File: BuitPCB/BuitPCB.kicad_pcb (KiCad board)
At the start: 2 copper layers, 100 x 100 mm, 7 parts, among them J1 USB_A, J2 RJ45_Abracon_ARJP11A-MASA-B-A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, U1 Teensy4.1

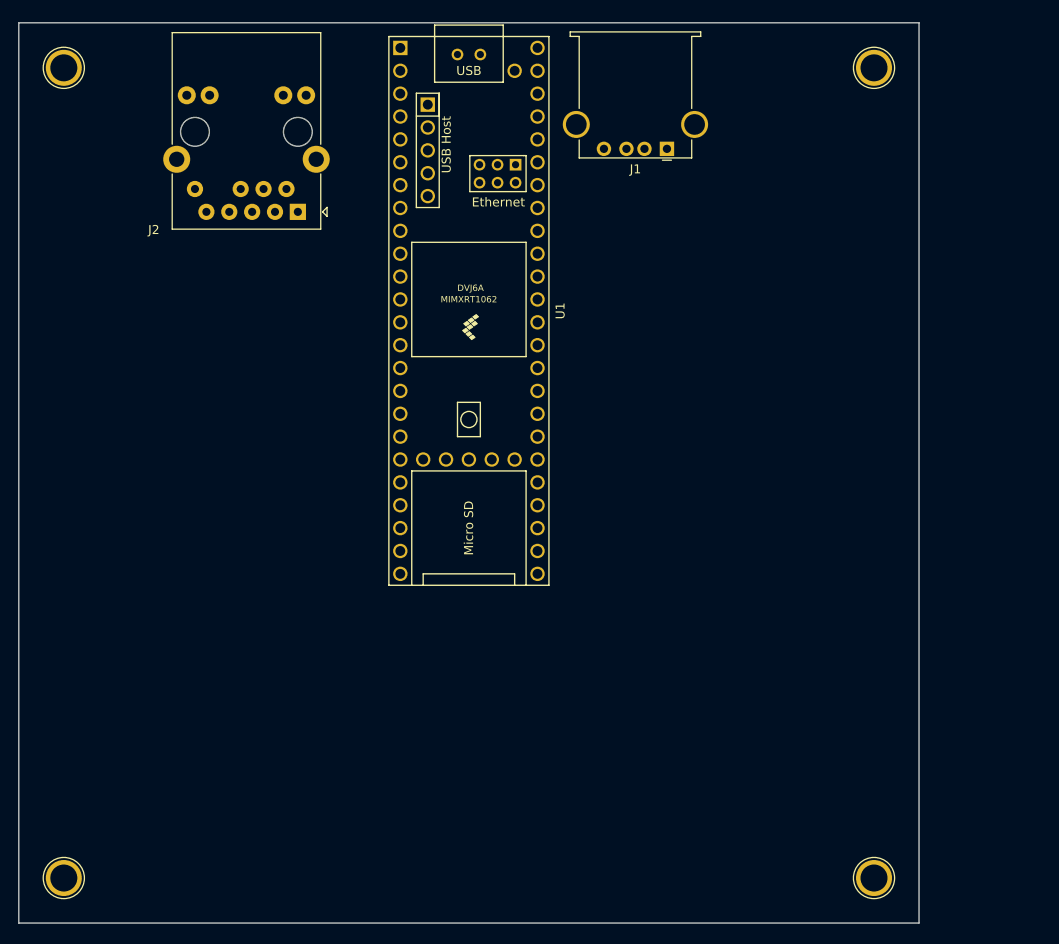
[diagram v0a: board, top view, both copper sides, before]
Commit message: Added sheets and connectors
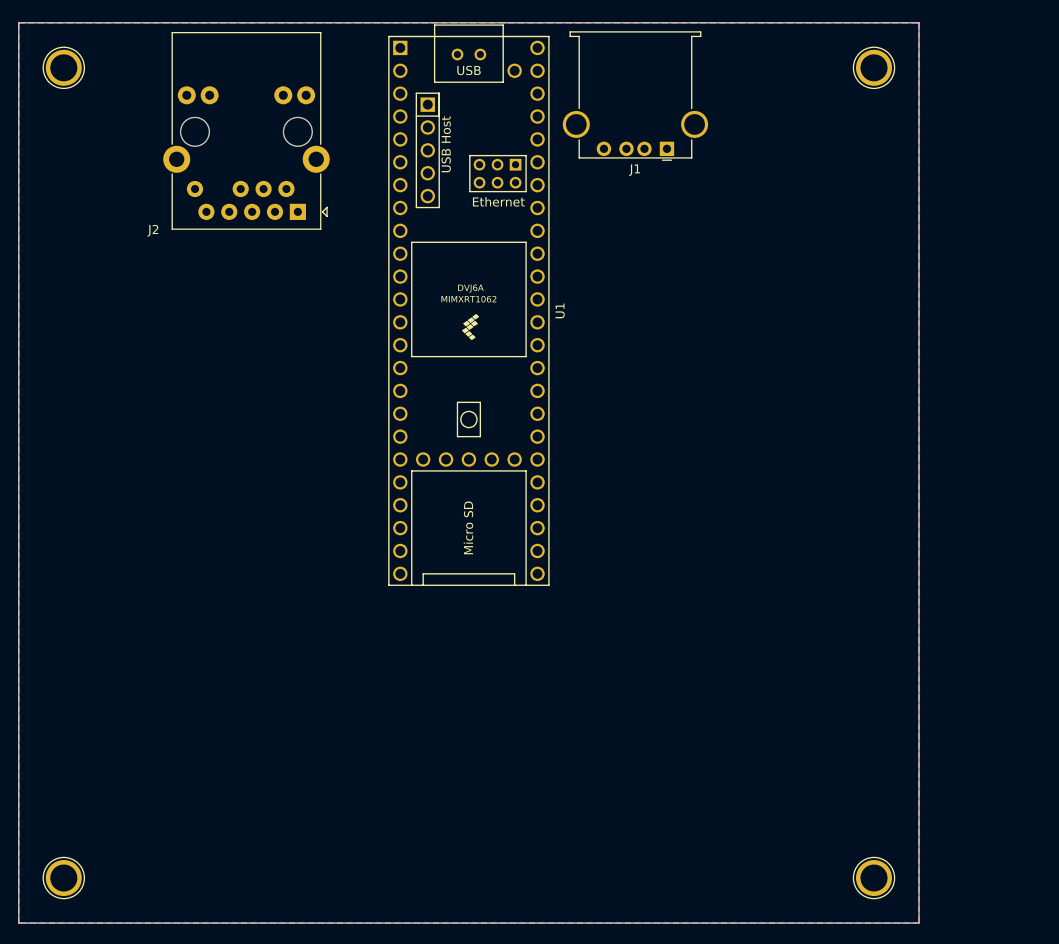
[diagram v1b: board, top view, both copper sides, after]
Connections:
- J1 pad 4: Net-(J1-Pad4) -> GND
- U1 pad 1: Net-(U1-Pad1) -> GND
- U1 pad 34: Net-(U1-Pad34) -> GND
- U1 pad 47: Net-(U1-Pad47) -> GND
- U1 pad 52: Net-(U1-Pad52) -> GND
- U1 pad 58: Net-(U1-Pad58) -> GND
- U1 pad 59: Net-(U1-Pad59) -> GND
- U1 pad 64: Net-(U1-Pad64) -> GND
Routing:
- added copper zone on B.Cu, net GND
- added copper zone on F.Cu, net GND

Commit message: Added most of components, few pending
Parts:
- removed REF** (x4): TestPoint_Plated_Hole_D3.0mm, TestPoint:TestPoint_Plated_Hole_D3.0mm
- added C1: C, Capacitor_SMD:C_0805_2012Metric, F.Cu at (178.0, 97.0)
- added C2: 100nF, Capacitor_SMD:C_0805_2012Metric, F.Cu at (176.5, 75.0)
- added C3: 100nF, Capacitor_SMD:C_0805_2012Metric, F.Cu at (181.0, 75.0)
- added C4: 100nF, Capacitor_SMD:C_0805_2012Metric, F.Cu at (176.5, 78.1)
- added D1: CD4148W, Diode_SMD:D_0805_2012Metric, F.Cu at (177.1, 110.7)
- added J10: Conn_01x06, Connector_JST:JST_XH_B6B-XH-A_1x06_P2.50mm_Vertical, F.Cu at (134.0, 117.0)
- added J11: Conn_01x04, Connector_JST:JST_XH_B4B-XH-A_1x04_P2.50mm_Vertical, F.Cu at (156.0, 126.0)
- added J12: Conn_01x04, Connector_JST:JST_XH_B4B-XH-A_1x04_P2.50mm_Vertical, F.Cu at (198.9, 122.3)
- added J13: Conn_01x04, Connector_JST:JST_XH_B4B-XH-A_1x04_P2.50mm_Vertical, F.Cu at (193.9, 130.1)
- added J14: Conn_01x04, Connector_JST:JST_XH_B4B-XH-A_1x04_P2.50mm_Vertical, F.Cu at (156.0, 136.0)
- added J15: Conn_01x04, Connector_JST:JST_XH_B4B-XH-A_1x04_P2.50mm_Vertical, F.Cu at (175.5, 134.0)
- added J16: Conn_01x04, Connector_JST:JST_XH_B4B-XH-A_1x04_P2.50mm_Vertical, F.Cu at (176.0, 124.0)
- added J17: Conn_01x04, Connector_JST:JST_XH_B4B-XH-A_1x04_P2.50mm_Vertical, F.Cu at (193.9, 137.9)
- added J18: Conn_01x04, Connector_JST:JST_XH_B4B-XH-A_1x04_P2.50mm_Vertical, F.Cu at (188.9, 145.7)
- added J3: USB_A, Connector_USB:USB_A_Stewart_SS-52100-001_Horizontal, F.Cu at (116.0, 136.0)
- added J4: AudioJack3, MiniJackConnector:MJ4435, F.Cu at (194.0, 53.0)
- added J6: AudioJack3, MiniJackConnector:MJ4435, F.Cu at (180.0, 53.0)
- added J7: Conn_01x06, Connector_JST:JST_XH_B6B-XH-A_1x06_P2.50mm_Vertical, F.Cu at (134.0, 125.0)
- added J8: Conn_01x06, Connector_JST:JST_XH_B6B-XH-A_1x06_P2.50mm_Vertical, F.Cu at (134.0, 135.0)
- added J9: Conn_01x06, Connector_JST:JST_XH_B6B-XH-A_1x06_P2.50mm_Vertical, F.Cu at (134.0, 108.0)
- added Q1: BSS138, Package_TO_SOT_SMD:SOT-23, F.Cu at (212.1, 121.2)
- added Q2: BSS138, Package_TO_SOT_SMD:SOT-23, F.Cu at (207.1, 129.0)
- added R1: 220R, Resistor_SMD:R_0805_2012Metric, F.Cu at (177.1, 113.7)
- added R2: 47R, Resistor_SMD:R_0805_2012Metric, F.Cu at (178.0, 100.0)
- added R3: 47R, Resistor_SMD:R_0805_2012Metric, F.Cu at (182.4, 97.0)
- added R4: 470R, Resistor_SMD:R_0805_2012Metric, F.Cu at (190.7, 98.8)
- added R5: 10K, Resistor_SMD:R_0805_2012Metric, F.Cu at (202.1, 143.8)
- added R6: 10K, Resistor_SMD:R_0805_2012Metric, F.Cu at (212.1, 125.0)
- added R7: 10K, Resistor_SMD:R_0805_2012Metric, F.Cu at (211.5, 128.2)
- added R8: 10K, Resistor_SMD:R_0805_2012Metric, F.Cu at (207.1, 132.8)
- added U2: 6N138, Package_DIP:DIP-8_W8.89mm_SMDSocket_LongPads, F.Cu at (136.0, 76.0)
- added U3: AP7361C-33E, Package_TO_SOT_SMD:SOT-223-3_TabPin2, F.Cu at (141.2, 95.0)
- added U4: SGTL5000XNAA3, Package_DFN_QFN:QFN-32-1EP_5x5mm_P0.5mm_EP3.6x3.6mm, F.Cu at (185.0, 86.0)
- J1: value USB_A -> DIN-5_180degree; footprint Connector_USB:USB_A_Stewart_SS-52100-001_Horizontal -> esp32s2:DJ005
- J2: value RJ45_Abracon_ARJP11A-MASA-B-A-EMU2 -> DIN-5_180degree; footprint Connector_RJ:RJ45_Abracon_ARJP11A-MA_Horizontal -> esp32s2:DJ005
- moved J1 38.6 mm to (136.0, 50.0), turned to 0 degrees
- moved J2 29.0 mm to (111.0, 50.0), turned to 0 degrees
- moved U1 11.0 mm to (161.0, 82.0)
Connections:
- J1 pad 4: GND -> Net-(J1-Pad4)

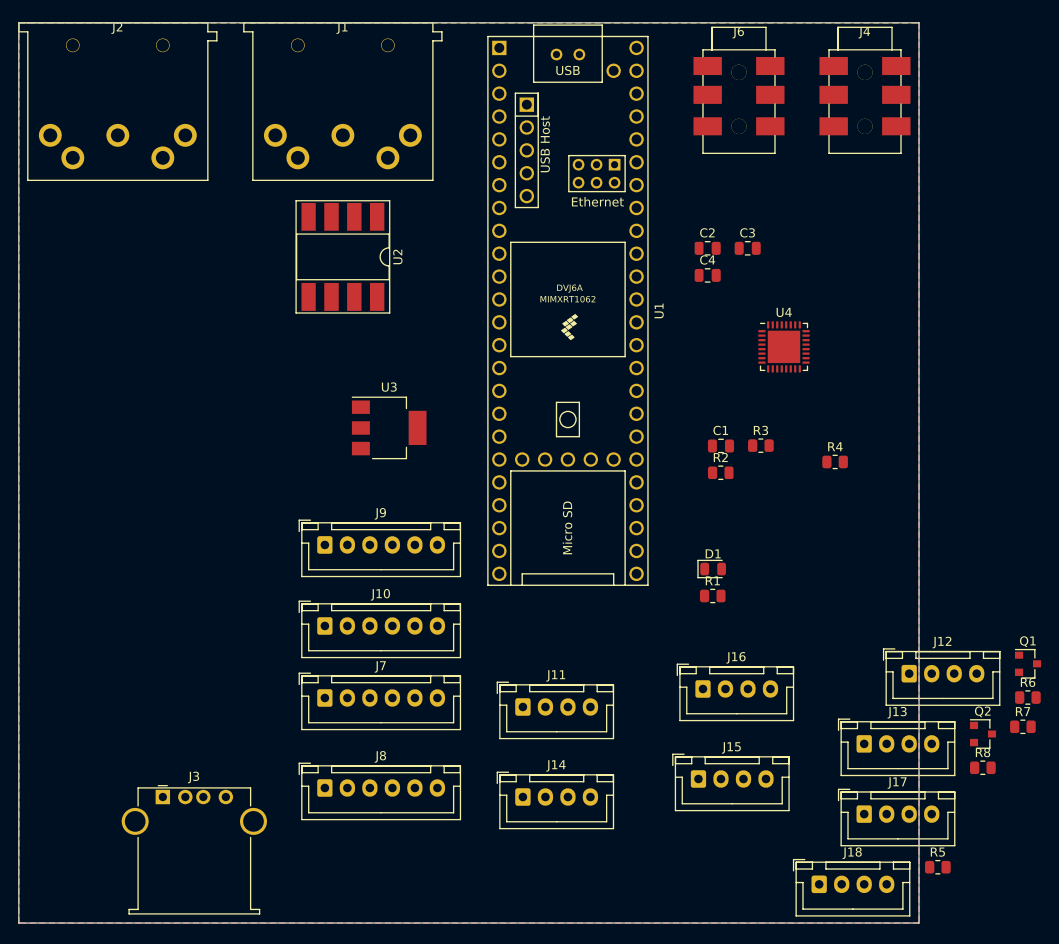
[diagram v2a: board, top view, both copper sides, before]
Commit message: Added sensors connectors
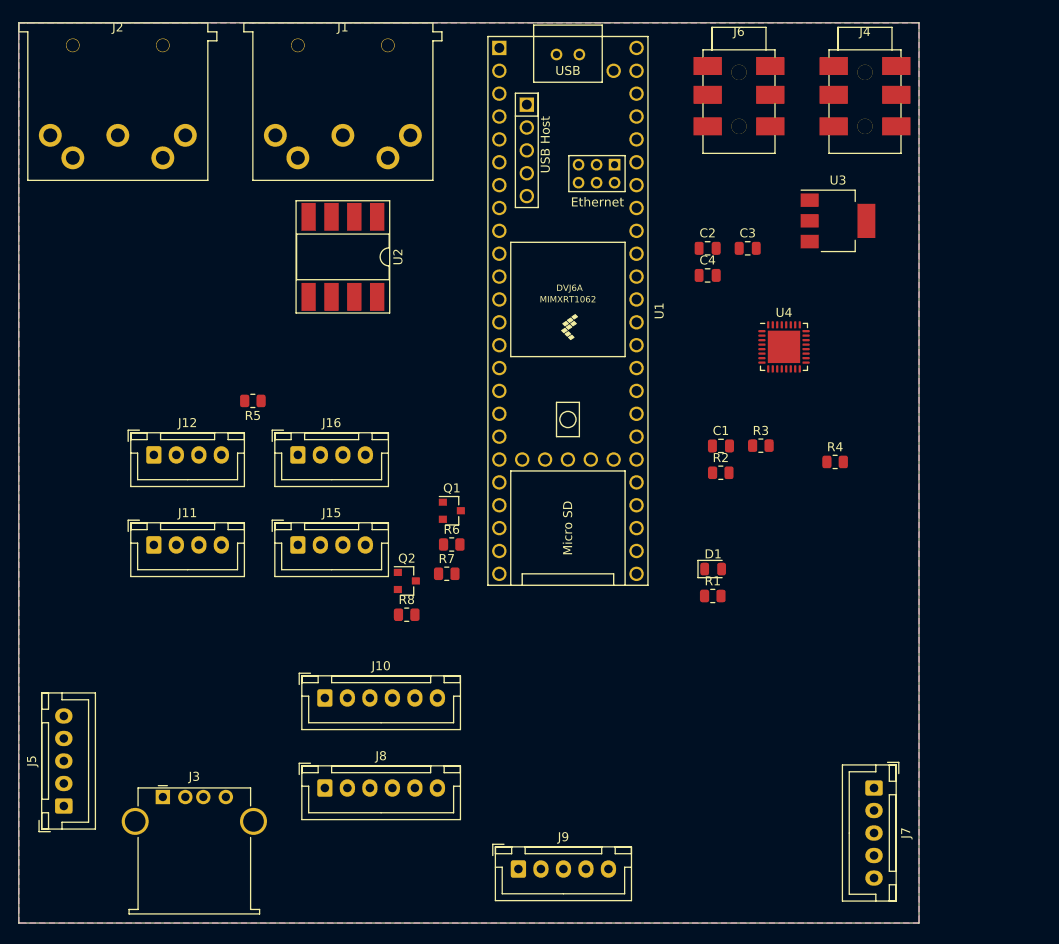
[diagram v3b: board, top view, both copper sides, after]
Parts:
- removed J13, J14, J17, J18: Conn_01x04, Connector_JST:JST_XH_B4B-XH-A_1x04_P2.50mm_Vertical
- added J5: LEFT SENS, Connector_JST:JST_XH_B5B-XH-A_1x05_P2.50mm_Vertical, F.Cu at (105.0, 137.0)
- J7: value Conn_01x06 -> RIGHT SENS; footprint Connector_JST:JST_XH_B6B-XH-A_1x06_P2.50mm_Vertical -> Connector_JST:JST_XH_B5B-XH-A_1x05_P2.50mm_Vertical
- J9: value Conn_01x06 -> CENTER SENS; footprint Connector_JST:JST_XH_B6B-XH-A_1x06_P2.50mm_Vertical -> Connector_JST:JST_XH_B5B-XH-A_1x05_P2.50mm_Vertical
- moved R5 92.0 mm to (126.0, 92.0), turned to 180 degrees
- moved J12 87.4 mm to (115.0, 98.0)
- moved Q1 66.2 mm to (148.1, 104.2)
- moved Q2 66.2 mm to (143.1, 112.0)
- moved R6 66.2 mm to (148.1, 108.0)
- moved R7 66.2 mm to (147.5, 111.2)
- moved R8 66.2 mm to (143.1, 115.8)
- moved J7 61.8 mm to (195.0, 135.0), turned to 270 degrees
- moved U3 54.9 mm to (191.0, 72.0)
- moved J16 52.0 mm to (131.0, 98.0)
- moved J15 51.5 mm to (131.0, 108.0)
- moved J11 44.8 mm to (115.0, 108.0)
- moved J9 41.9 mm to (155.5, 144.0)
- moved J10 8.00 mm to (134.0, 125.0)
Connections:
- net Net-(U1-Pad55) renamed USB_HOST_5V
- J3 pad 2: Net-(J3-Pad2) -> USB_HOST_D-
- J3 pad 3: Net-(J3-Pad3) -> USB_HOST_D+
- J3 pad 5: Net-(J3-Pad5) -> GND
- J7 pad 2: SPI_MISO -> SENS_I2C_SCL
- J7 pad 3: SPI_SCK -> SENS_I2C_SDA
- J7 pad 4: SPI_MOSI -> SENS_XOUT_RIGHT
- J7 pad 5: SPI_CS3 -> GND
- J9 pad 2: SPI_MISO -> SENS_I2C_SCL
- J9 pad 3: SPI_SCK -> SENS_I2C_SDA
- J9 pad 4: SPI_MOSI -> SENS_XOUT_CENTER
- J9 pad 5: SPI_CS4 -> GND
- R3 pad 1: MIDI_IN -> MIDI_OUT
- U1 pad 10: Net-(U1-Pad10) -> I2S_DOUT
- U1 pad 15: Net-(U1-Pad15) -> +3V3
- U1 pad 2: Net-(U1-Pad2) -> MIDI_IN
- U1 pad 3: Net-(U1-Pad3) -> MIDI_OUT
- U1 pad 40: Net-(U1-Pad40) -> I2C_SDA_3V3
- U1 pad 41: Net-(U1-Pad41) -> I2C_SCL_3V3
- U1 pad 42: Net-(U1-Pad42) -> I2S_LRCLK
- U1 pad 43: Net-(U1-Pad43) -> I2S_SCLK
- U1 pad 45: Net-(U1-Pad45) -> I2S_MCLK
- U1 pad 51: Net-(U1-Pad51) -> +3V3
- U1 pad 56: Net-(U1-Pad56) -> USB_HOST_D-
- U1 pad 57: Net-(U1-Pad57) -> USB_HOST_D+
- U1 pad 9: Net-(U1-Pad9) -> I2S_DIN

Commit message: Updated adding battery management sheet and componnents to PCB
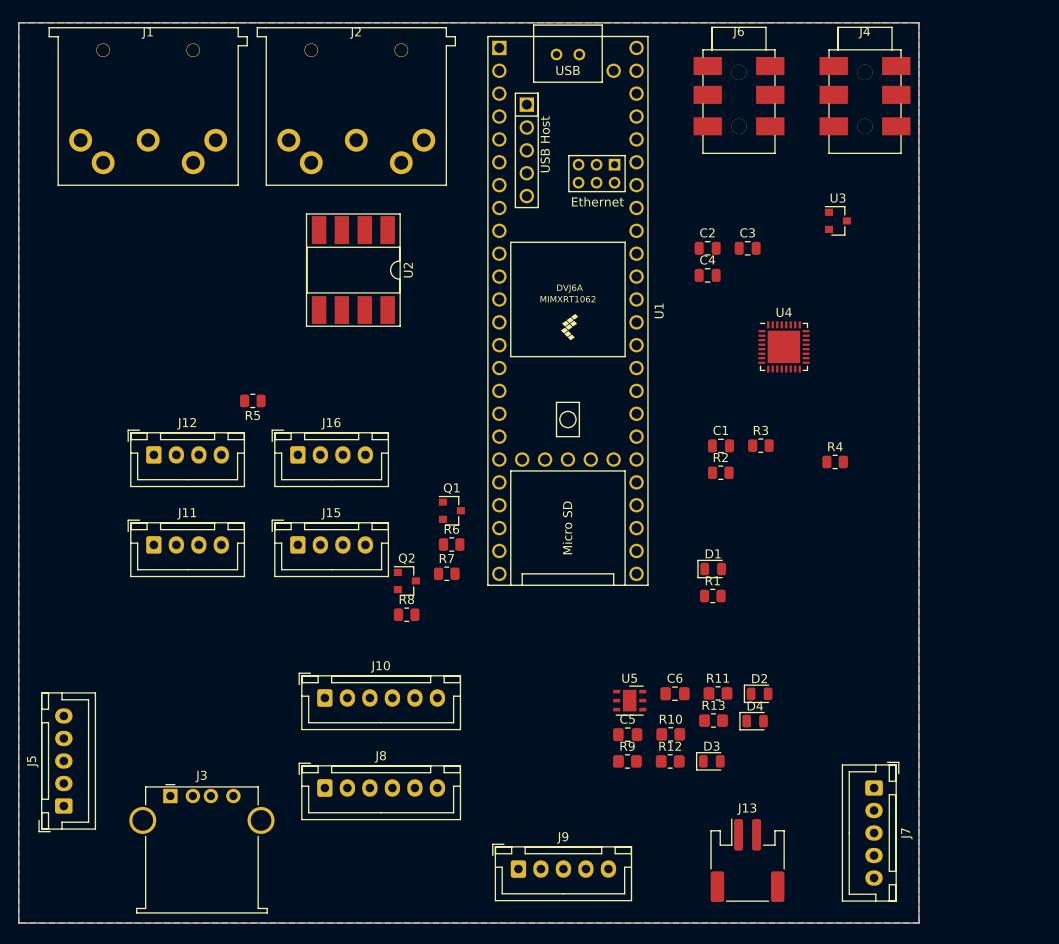
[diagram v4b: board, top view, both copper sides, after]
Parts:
- added C5: 4.7uF, Capacitor_SMD:C_0805_2012Metric_Pad1.18x1.45mm_HandSolder, F.Cu at (167.6, 129.1)
- added C6: 4.7uF, Capacitor_SMD:C_0805_2012Metric_Pad1.18x1.45mm_HandSolder, F.Cu at (172.9, 124.5)
- added D2: LED, LED_SMD:LED_0805_2012Metric, F.Cu at (182.3, 124.5)
- added D3: LED, LED_SMD:LED_0805_2012Metric, F.Cu at (177.0, 132.0)
- added D4: LED, LED_SMD:LED_0805_2012Metric, F.Cu at (181.8, 127.6)
- added J13: Conn_01x02, Connector_JST:JST_PH_S2B-PH-SM4-TB_1x02-1MP_P2.00mm_Horizontal, F.Cu at (181.0, 143.1)
- added R10: 1KR, Resistor_SMD:R_0805_2012Metric_Pad1.20x1.40mm_HandSolder, F.Cu at (172.4, 129.0)
- added R11: 3K3R, Resistor_SMD:R_0805_2012Metric_Pad1.20x1.40mm_HandSolder, F.Cu at (177.7, 124.5)
- added R12: 2KR, Resistor_SMD:R_0805_2012Metric_Pad1.20x1.40mm_HandSolder, F.Cu at (172.4, 132.1)
- added R13: 1KR, Resistor_SMD:R_0805_2012Metric_Pad1.20x1.40mm_HandSolder, F.Cu at (177.2, 127.5)
- added R9: 1KR, Resistor_SMD:R_0805_2012Metric_Pad1.20x1.40mm_HandSolder, F.Cu at (167.6, 132.1)
- added U5: STBC08, Package_DFN_QFN:DFN-6-1EP_3x3mm_P1mm_EP1.5x2.4mm, F.Cu at (167.9, 125.3)
- U3: footprint Package_TO_SOT_SMD:SOT-223-3_TabPin2 -> Package_TO_SOT_SMD:SOT-23
- moved J2 26.5 mm to (137.5, 50.5)
- moved J1 21.6 mm to (114.4, 50.5)
- moved U2 1.87 mm to (137.2, 77.5)
- moved J3 0.85 mm to (116.8, 135.9)
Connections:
- U1 pad 49: Net-(U1-Pad49) -> V_USB

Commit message: Updated adding esp8266 transceiver module
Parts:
- added U6: ESP82SerialTransc, ESP32-Footprints:ESP82SerialTransceiver, F.Cu at (126.7, 89.7)
- moved J7 16.4 mm to (196.8, 118.7)
- moved U4 15.2 mm to (191.8, 72.4), turned to 90 degrees
- moved C4 11.3 mm to (185.4, 85.1)
- moved C3 11.1 mm to (190.8, 80.1)
- moved C2 10.2 mm to (185.4, 80.1)
- moved U3 7.18 mm to (184.2, 69.8), turned to 90 degrees
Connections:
- U1 pad 36: Net-(U1-Pad36) -> ESP8266_UART_RX
- U1 pad 37: Net-(U1-Pad37) -> ESP8266_UART_TX
- U1 pad 38: Net-(U1-Pad38) -> SENS_I2C_SCL
- U1 pad 39: Net-(U1-Pad39) -> SENS_I2C_SDA
- U1 pad 4: Net-(U1-Pad4) -> SENS_XOUT_LEFT
- U1 pad 5: Net-(U1-Pad5) -> SENS_XOUT_CENTER
- U1 pad 6: Net-(U1-Pad6) -> SENS_XOUT_RIGHT
